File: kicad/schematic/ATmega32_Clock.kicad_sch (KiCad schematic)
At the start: 20 parts, among them J1 USART_HDR, J2 ISP_HDR, SW1 RESET, SW2 SET, SW3 INCREMENT, SW4 CLOCK_RESET, U1 ATmega32-16PU, Y1 8MHz

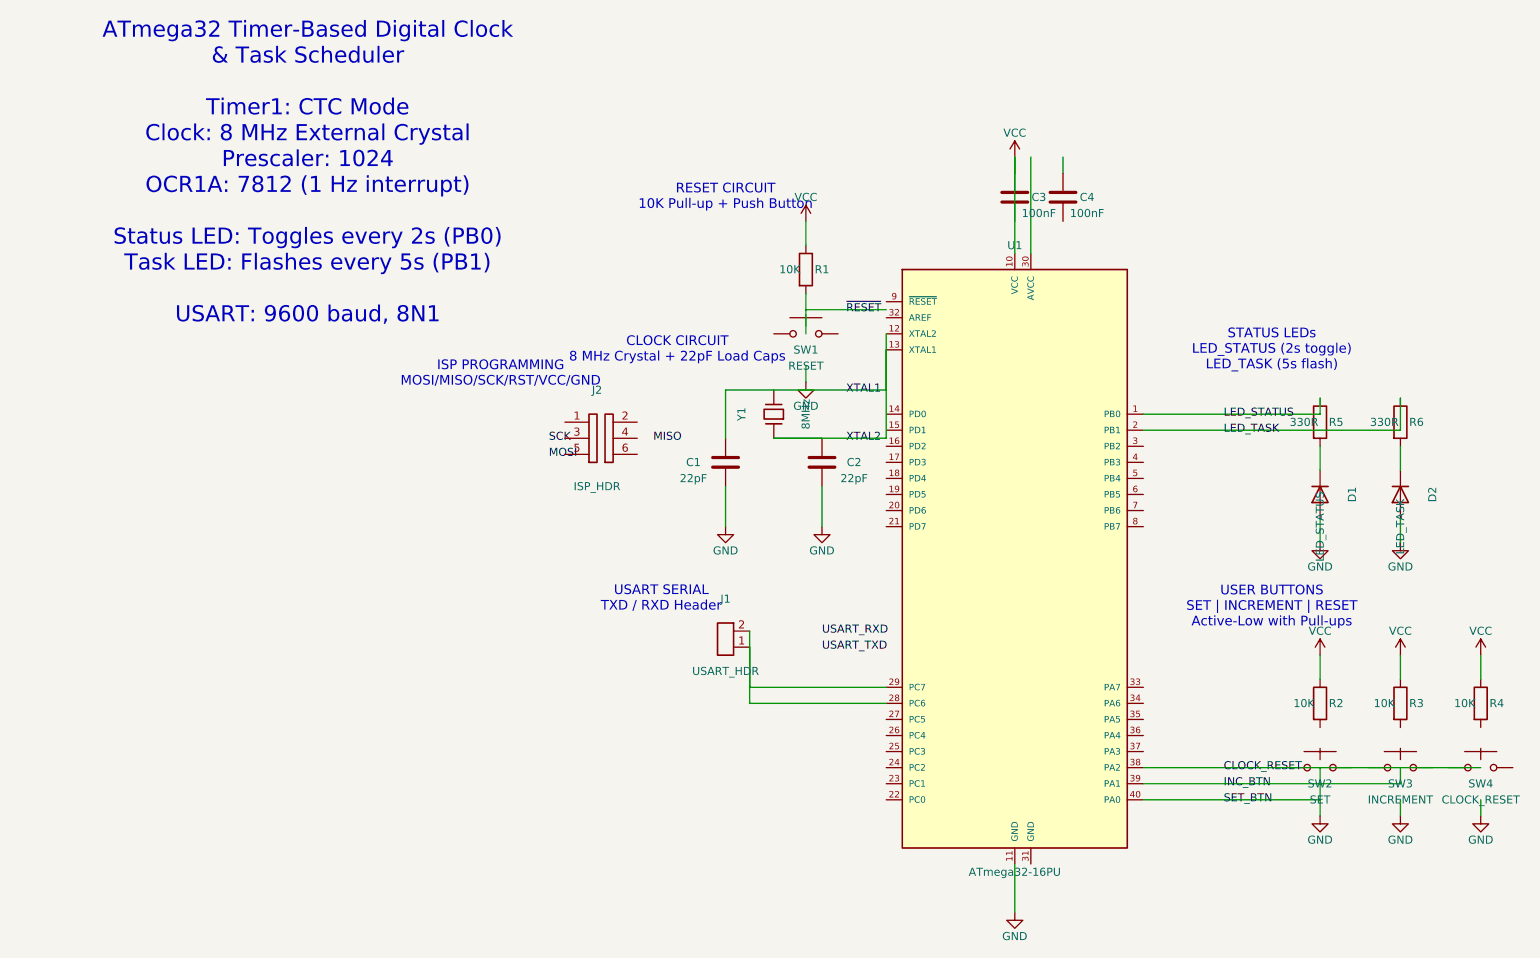
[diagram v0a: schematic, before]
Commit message: Implemented 10ms Timer1 Extension Task (100% score update)
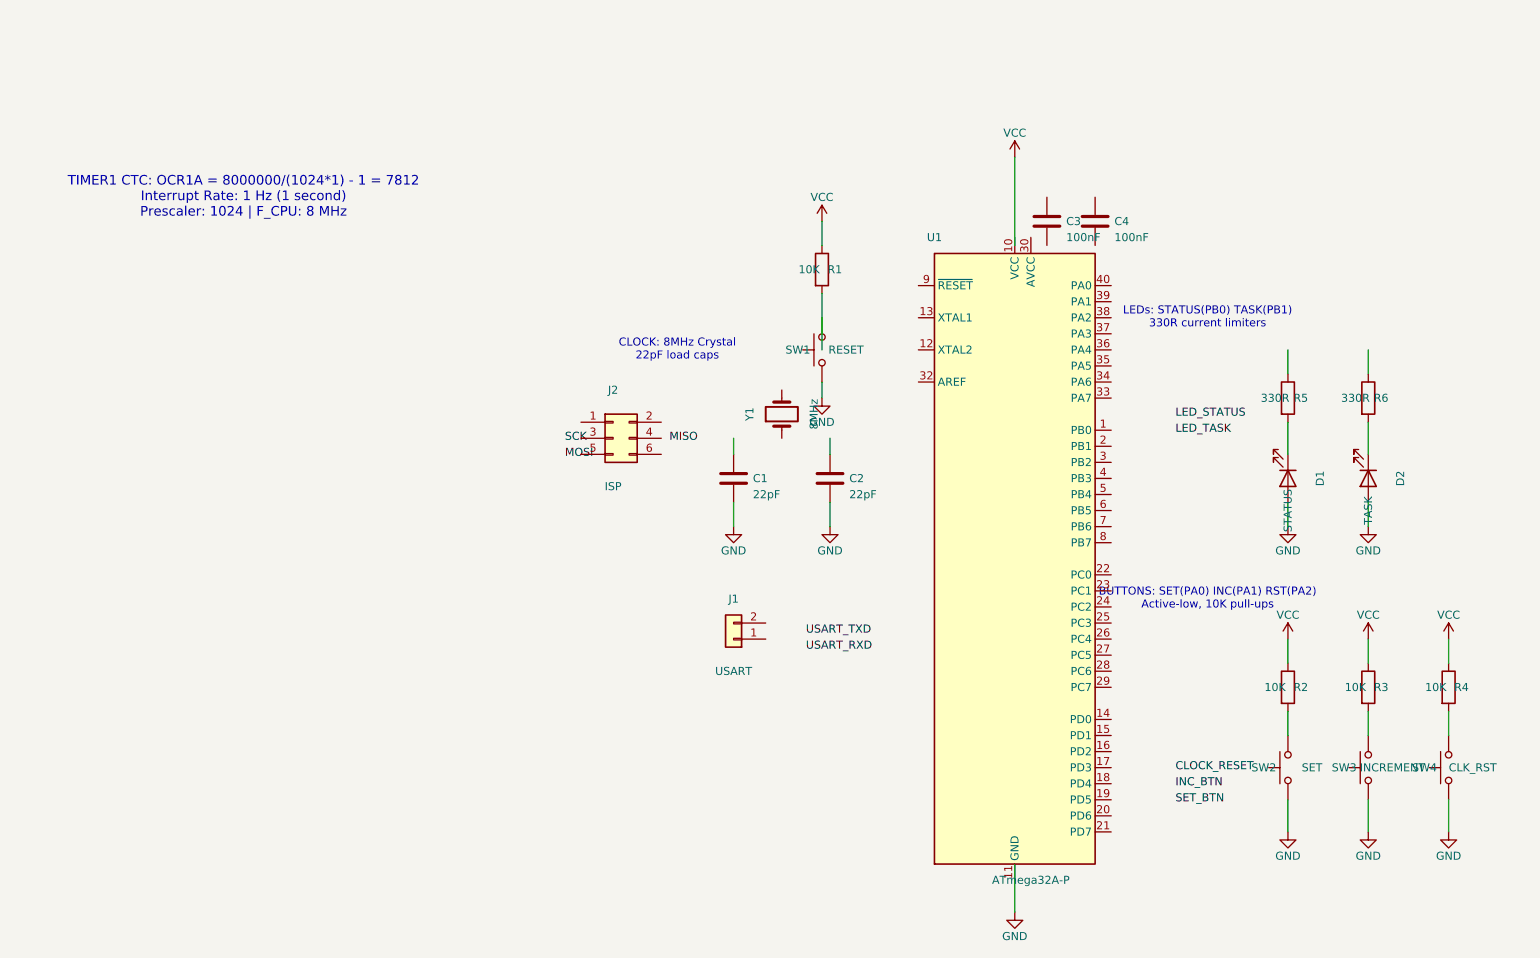
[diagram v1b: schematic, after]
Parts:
- removed U1: ATmega32-16PU, Package_DIP:DIP-40_W15.24mm, symbol MCU_Microchip_ATmega:ATmega32-16PU
- added U1: ATmega32A-P, Package_DIP:DIP-40_W15.24mm, symbol MCU_Microchip_ATmega:ATmega32A-P
- D1: value LED_STATUS -> STATUS
- D2: value LED_TASK -> TASK
- J1: value USART_HDR -> USART
- J2: value ISP_HDR -> ISP
- SW4: value CLOCK_RESET -> CLK_RST
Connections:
- net ~{RESET} is gone; now on an unnamed net: R1.2
- net GND: now also SW1.1, SW2.1, SW3.1, SW4.1
- net LED_STATUS: no longer R5.1
- net LED_TASK: no longer R6.1
- net VCC: no longer C3.1
- net at J1.1 (Pin_1): no longer J1.2 (Pin_2)
- net at R2.2: now also SW2.2
- net at R3.2: now also SW3.2
- net at R4.2: now also SW4.2
- removed net XTAL1: C1.1, C2.1, Y1.1, Y1.2
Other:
- note added: "BUTTONS: SET(PA0) INC(PA1) RST(PA2) Active-low, 10K pull-ups"
- note added: "CLOCK: 8MHz Crystal 22pF load caps"
- note added: "LEDs: STATUS(PB0) TASK(PB1) 330R current limiters"
- note added: "TIMER1 CTC: OCR1A = 8000000/(1024*1) - 1 = 7812 Interrupt Rate: 1 Hz (1 second) Prescaler: 1024 | F_CPU: 8 MHz"
- note removed: "ATmega32 Timer-Based Digital Clock & Task Scheduler Timer1: CTC Mode Clock: 8 MHz External Crystal Prescaler: 1024 OCR1A: 7812 (1 Hz interrupt) Status LED: Toggles every 2s (PB0) Task LED: Flashes every 5s (PB1) USART: 9600 baud, 8N1"
- note removed: "CLOCK CIRCUIT 8 MHz Crystal + 22pF Load Caps"
- note removed: "ISP PROGRAMMING MOSI/MISO/SCK/RST/VCC/GND"
- note removed: "RESET CIRCUIT 10K Pull-up + Push Button"
- note removed: "STATUS LEDs LED_STATUS (2s toggle) LED_TASK (5s flash)"
- note removed: "USART SERIAL TXD / RXD Header"
- note removed: "USER BUTTONS SET | INCREMENT | RESET Active-Low with Pull-ups"
- company: (none) -> CT_321 PBL Project 08

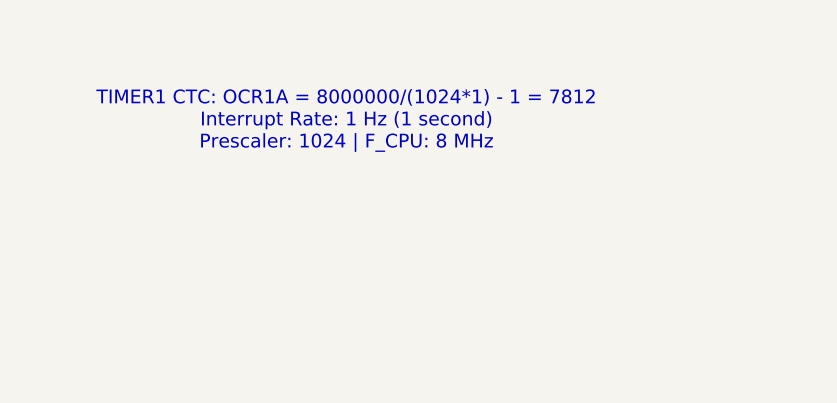
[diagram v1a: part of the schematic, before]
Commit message: Updated schematic timer annotations to correctly reflect the new 100Hz/10ms Prescaler 64 firmware architecture.
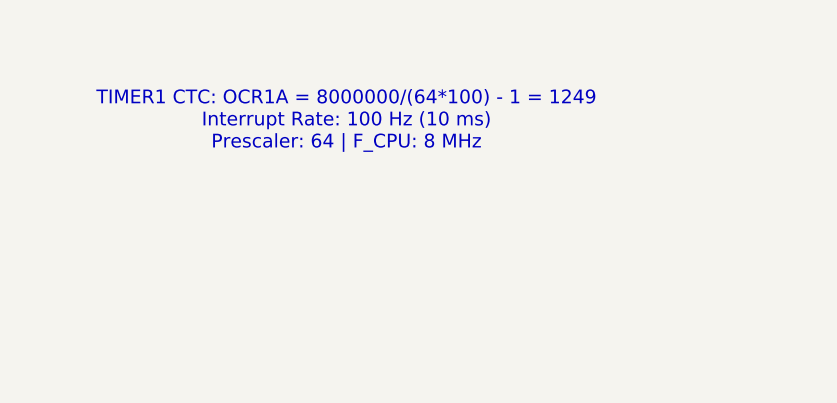
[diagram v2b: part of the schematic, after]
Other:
- note added: "TIMER1 CTC: OCR1A = 8000000/(64*100) - 1 = 1249 Interrupt Rate: 100 Hz (10 ms) Prescaler: 64 | F_CPU: 8 MHz"
- note removed: "TIMER1 CTC: OCR1A = 8000000/(1024*1) - 1 = 7812 Interrupt Rate: 1 Hz (1 second) Prescaler: 1024 | F_CPU: 8 MHz"
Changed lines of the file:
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@@
     (rev "1.0")
     (company "CT_321 PBL Project 08")
-    (comment 1 "Timer1 CTC | 8MHz Crystal | Prescaler 1024 | OCR1A=7812 | 1Hz Interrupt")
+    (comment 1 "Timer1 CTC | 8MHz Crystal | Prescaler 64 | OCR1A=1249 | 100Hz Interrupt")
     (comment 2 "Status LED: PB0 toggles 2s | Task LED: PB1 flashes 5s | USART 9600")
   )
@@
   (wire (pts (xy 121.92 73.66) (xy 121.92 76.2)) (stroke (width 0) (type default)))
   ;; ============= Text annotations =============
-  (text "TIMER1 CTC: OCR1A = 8000000/(1024*1) - 1 = 7812\nInterrupt Rate: 1 Hz (1 second)\nPrescaler: 1024 | F_CPU: 8 MHz"
+  (text "TIMER1 CTC: OCR1A = 8000000/(64*100) - 1 = 1249\nInterrupt Rate: 100 Hz (10 ms)\nPrescaler: 64 | F_CPU: 8 MHz"
     (at 30.48 44.45 0) (effects (font (size 1.524 1.524)))
   )
